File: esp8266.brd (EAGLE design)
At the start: 29.5 x 28.6 mm, 33 parts, among them IC1 74LVC1G08DBV, U1 FT232RL-BASICSSOP, U2 SPX3819M5-L33

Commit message: Change the second VIN to ground
It's more useful that way.
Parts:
- removed U$1: P-CHANNEL-MOSFET, GeekAmmo:SOT23-3
- added PFET1: P-CHANNEL-MOSFET, GeekAmmo:SOT23-3
- added PFET2: BSS84, transistor-small-signal:SOT23
- moved D2 3.35 mm to (23.0, 71.8), turned to 180 degrees
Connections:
- new net N$5: BAT.1, PFET2.3
- net GND: now also BAT.2, JP3.1, PFET2.1; no longer BAT.1
- net N$2: now also PFET1.1; no longer U$1.1
- net VBAT: now also PFET1.3, PFET2.2; no longer BAT.2, U$1.3
- net VIN: no longer JP3.1
- net VRIN: now also PFET1.2; no longer U$1.2
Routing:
- net GND: track 53.9 -> 18.4 mm, vias 17 -> 21
- net N$5: track 0.00 -> 10.3 mm
- net VRIN: track 33.3 -> 42.9 mm, vias 3 -> 4
- net RTS: track 42.0 -> 50.4 mm, vias 2 -> 4
- net N$2: track 75.5 -> 80.8 mm, vias 2 -> 7
- net VBAT: track 17.2 -> 21.7 mm, vias 0 -> 2
- net RX: track 39.4 -> 43.0 mm, vias 4 -> 2
- net VIN: track 72.8 -> 71.8 mm
- net 3V3: track 100.8 -> 101.4 mm
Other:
- board text added: "28.10.2015.HSF+LF"
- board text removed: "29.09.2015.HSF+LF"

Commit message: New routing
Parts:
- moved PFET2 1.42 mm to (20.3, 76.8)
- turned C1 to 0 degrees
- turned C4 to 90 degrees
- turned R13 to 90 degrees
- turned R3 to 180 degrees
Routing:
- net VRIN: track 42.9 -> 92.8 mm, vias 4 -> 6
- net VIN: track 71.8 -> 40.6 mm, vias 3 -> 2
- net RX: track 43.0 -> 19.2 mm, vias 2 -> 1
- net 3V3: track 101.4 -> 83.3 mm
- net CH_PD: track 15.1 -> 28.3 mm
- net GND: track 18.4 -> 5.17 mm, vias 21 -> 14
- net TX: track 38.4 -> 27.1 mm, vias 2 -> 1
- net RTS: track 50.4 -> 40.8 mm, vias 4 -> 1
- net RXLED: track 19.6 -> 11.0 mm
- net D-: track 10.7 -> 15.4 mm
- net VBAT: track 21.7 -> 26.5 mm
- net N$8: track 11.8 -> 7.37 mm
- net P14: track 12.7 -> 16.8 mm, vias 1 -> 0
- net N$4: track 11.8 -> 9.12 mm
- net ADC: track 17.1 -> 19.7 mm, vias 0 -> 2
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
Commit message: Finished routing
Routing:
- net RX: track 19.2 -> 20.7 mm
- net GND: track 5.17 -> 4.57 mm
- net P12: track 19.0 -> 18.5 mm, vias 1 -> 0
- net 3V3: track 83.3 -> 83.4 mm, vias 3 -> 5

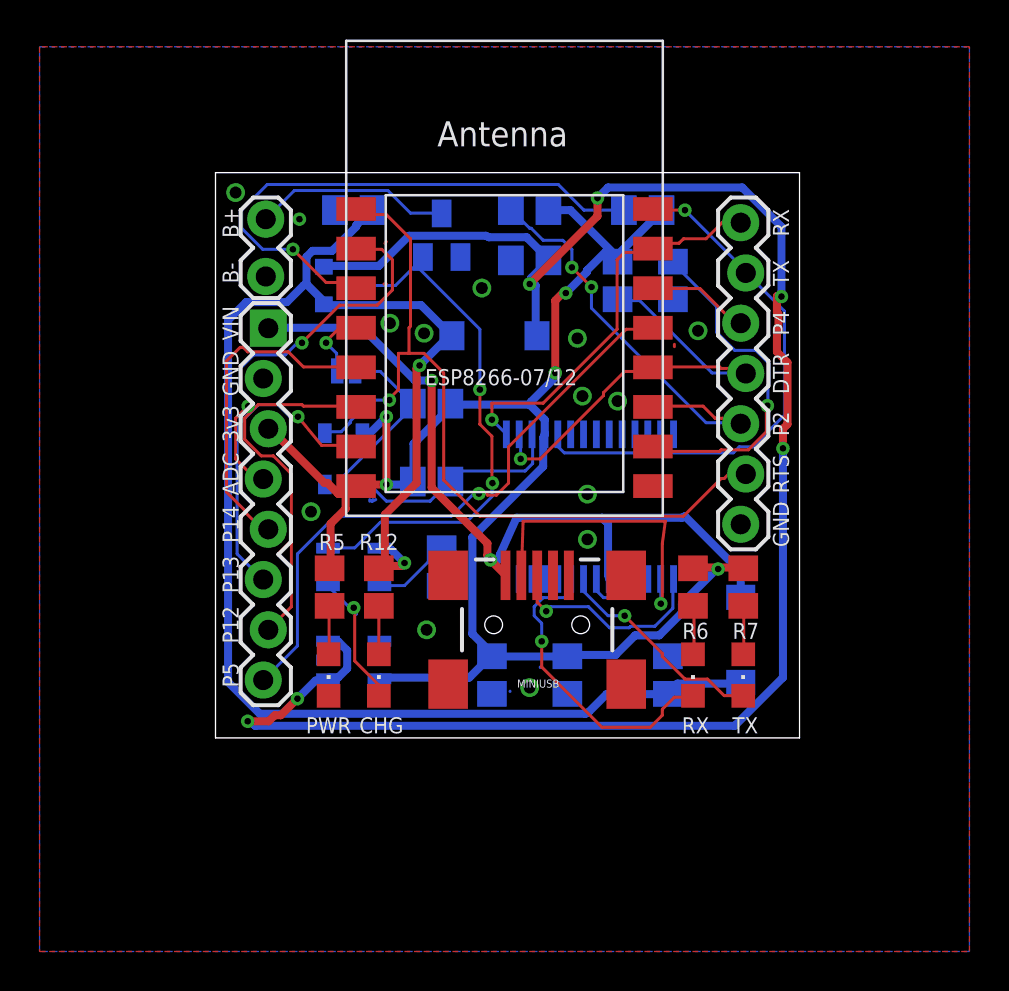
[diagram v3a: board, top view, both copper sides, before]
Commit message: Fix clearence issues
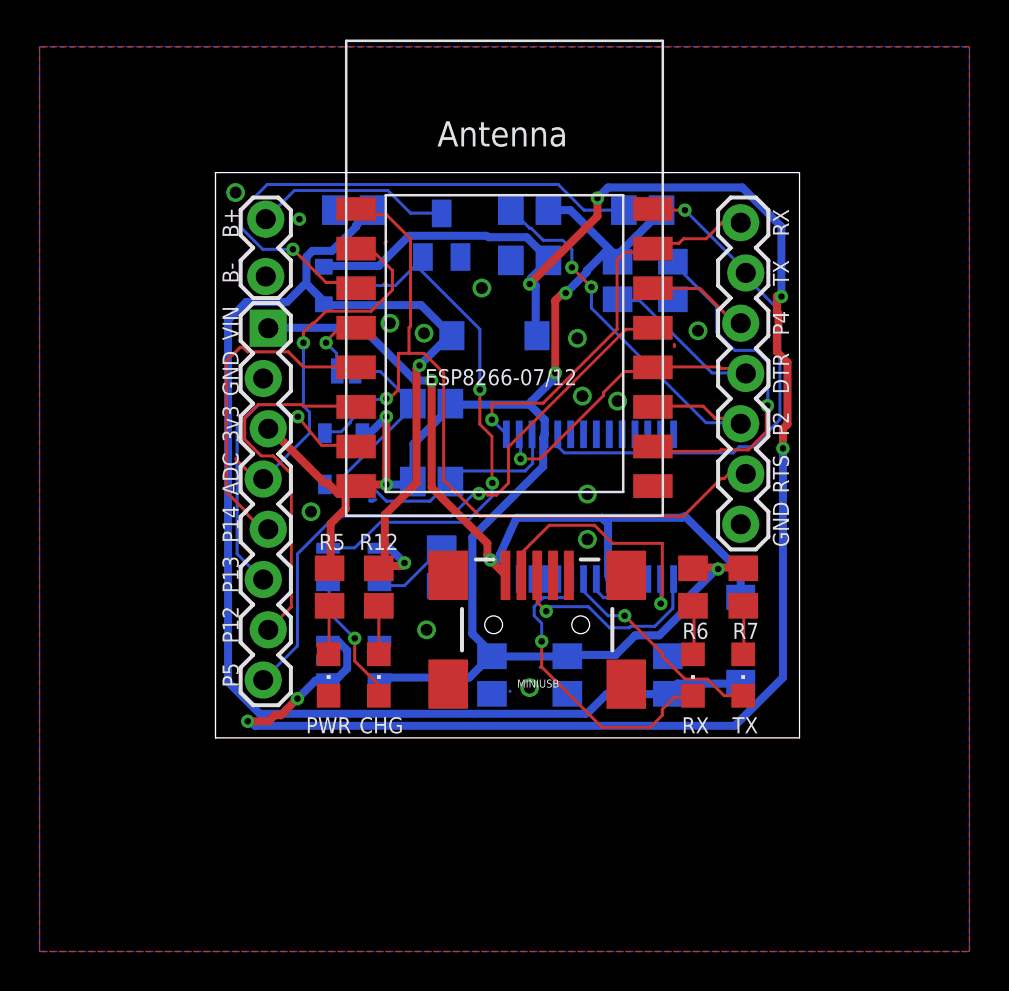
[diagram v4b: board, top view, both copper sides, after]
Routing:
- net ADC: track 19.8 -> 19.0 mm, vias 2 -> 1
- net D-: track 15.4 -> 14.7 mm
- net N$8: track 7.37 -> 6.70 mm
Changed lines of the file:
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@@
 <wire x1="35.3568" y1="66.1416" x2="35.052" y2="65.8368" width="0.1524" layer="16"/>
 <wire x1="36.0426" y1="66.1416" x2="35.3568" y2="66.1416" width="0.1524" layer="16"/>
-<wire x1="37.6428" y1="67.7418" x2="36.0426" y2="66.1416" width="0.1524" layer="16"/>
-<wire x1="37.6428" y1="72.9996" x2="37.6428" y2="67.7418" width="0.1524" layer="16"/>
-<wire x1="35.7378" y1="74.9046" x2="37.6428" y2="72.9996" width="0.1524" layer="16"/>
 <wire x1="26.2128" y1="66.7512" x2="26.188" y2="66.775" width="0.1524" layer="16"/>
 <wire x1="35.7378" y1="74.9046" x2="35.687" y2="74.93" width="0.1524" layer="16"/>
@@
 <wire x1="35.7378" y1="74.9808" x2="35.687" y2="74.93" width="0.1524" layer="16"/>
 <via x="32.6136" y="78.105" extent="1-16" drill="0.3302"/>
+<wire x1="37.4142" y1="67.5132" x2="36.0426" y2="66.1416" width="0.1524" layer="16"/>
+<wire x1="37.4142" y1="72.9996" x2="37.4142" y2="67.5132" width="0.1524" layer="16"/>
+<wire x1="35.7378" y1="74.676" x2="37.4142" y2="72.9996" width="0.1524" layer="16"/>
+<wire x1="35.7378" y1="74.8284" x2="35.7378" y2="74.676" width="0.1524" layer="16"/>
+<wire x1="35.7378" y1="74.8284" x2="35.687" y2="74.93" width="0.1524" layer="16"/>
 </signal>
 <signal name="P14">
@@
 <contactref element="ESP8266-07/12" pad="2"/>
 <contactref element="JP1" pad="4"/>
-<wire x1="17.2974" y1="76.1238" x2="16.002" y2="76.1238" width="0.1524" layer="1"/>
-<wire x1="17.8308" y1="75.5904" x2="17.2974" y2="76.1238" width="0.1524" layer="1"/>
-<wire x1="17.8308" y1="74.0664" x2="17.8308" y2="75.5904" width="0.1524" layer="1"/>
-<wire x1="17.0688" y1="73.3044" x2="17.8308" y2="74.0664" width="0.1524" layer="1"/>
-<wire x1="15.1638" y1="73.3044" x2="17.0688" y2="73.3044" width="0.1524" layer="1"/>
-<wire x1="13.2588" y1="71.3994" x2="15.1638" y2="73.3044" width="0.1524" layer="1"/>
-<wire x1="13.0302" y1="71.3994" x2="13.2588" y2="71.3994" width="0.1524" layer="16"/>
-<wire x1="12.4206" y1="70.7898" x2="13.0302" y2="71.3994" width="0.1524" layer="16"/>
-<wire x1="10.8204" y1="70.7898" x2="12.4206" y2="70.7898" width="0.1524" layer="16"/>
-<wire x1="10.1346" y1="70.104" x2="10.8204" y2="70.7898" width="0.1524" layer="16"/>
 <wire x1="10.8966" y1="64.5414" x2="9.906" y2="65.532" width="0.1524" layer="1"/>
 <wire x1="11.2776" y1="64.5414" x2="10.8966" y2="64.5414" width="0.1524" layer="1"/>
+<wire x1="11.2776" y1="64.5414" x2="11.303" y2="64.516" width="0.1524" layer="1"/>
+<wire x1="16.764" y1="76.1238" x2="16.002" y2="76.1238" width="0.1524" layer="1"/>
+<wire x1="17.8308" y1="75.057" x2="16.764" y2="76.1238" width="0.1524" layer="1"/>
+<wire x1="17.8308" y1="74.0664" x2="17.8308" y2="75.057" width="0.1524" layer="1"/>
+<wire x1="16.764" y1="72.9996" x2="17.8308" y2="74.0664" width="0.1524" layer="1"/>
+<wire x1="14.478" y1="72.9996" x2="16.764" y2="72.9996" width="0.1524" layer="1"/>
+<wire x1="13.8684" y1="72.39" x2="14.478" y2="72.9996" width="0.1524" layer="1"/>
+<wire x1="13.7922" y1="72.39" x2="13.8684" y2="72.39" width="0.1524" layer="1"/>
+<wire x1="13.335" y1="71.9328" x2="13.7922" y2="72.39" width="0.1524" layer="1"/>
+<wire x1="13.335" y1="71.3994" x2="13.335" y2="71.9328" width="0.1524" layer="1"/>
+<wire x1="13.335" y1="68.199" x2="13.335" y2="71.3994" width="0.1524" layer="16"/>
+<wire x1="13.6398" y1="67.8942" x2="13.335" y2="68.199" width="0.1524" layer="16"/>
+<wire x1="13.6398" y1="66.8274" x2="13.6398" y2="67.8942" width="0.1524" layer="16"/>
+<wire x1="11.3538" y1="64.5414" x2="13.6398" y2="66.8274" width="0.1524" layer="16"/>
 <wire x1="16.002" y1="76.1238" x2="15.995" y2="76.16" width="0.1524" layer="1"/>
-<wire x1="11.2776" y1="64.5414" x2="11.303" y2="64.516" width="0.1524" layer="1"/>
-<via x="13.2588" y="71.3994" extent="1-16" drill="0.3302"/>
-<via x="10.541" y="68.199" extent="1-16" drill="0.3302"/>
-<wire x1="9.906" y1="67.5894" x2="10.5156" y2="68.199" width="0.1524" layer="1"/>
-<wire x1="9.906" y1="65.532" x2="9.906" y2="67.5894" width="0.1524" layer="1"/>
-<wire x1="10.5156" y1="68.199" x2="10.541" y2="68.199" width="0.1524" layer="1"/>
-<wire x1="10.5156" y1="68.6562" x2="10.5156" y2="68.199" width="0.1524" layer="16"/>
-<wire x1="10.1346" y1="69.0372" x2="10.5156" y2="68.6562" width="0.1524" layer="16"/>
-<wire x1="10.1346" y1="70.104" x2="10.1346" y2="69.0372" width="0.1524" layer="16"/>
-<wire x1="10.5156" y1="68.199" x2="10.541" y2="68.199" width="0.1524" layer="16"/>
+<wire x1="11.3538" y1="64.5414" x2="11.303" y2="64.516" width="0.1524" layer="16"/>
+<via x="13.335" y="71.3994" extent="1-16" drill="0.3302"/>
 </signal>
 <signal name="WDOG">
@@
 <contactref element="CHG" pad="C"/>
 <contactref element="MCP73831" pad="1"/>
-<wire x1="16.002" y1="57.6834" x2="15.875" y2="58.0136" width="0.1524" layer="16"/>
-<wire x1="14.6304" y1="59.055" x2="16.002" y2="57.6834" width="0.1524" layer="16"/>
 <wire x1="14.6304" y1="59.055" x2="14.5749" y2="59.121" width="0.1524" layer="16"/>
-<via x="15.875" y="58.0136" extent="1-16" drill="0.3302"/>
 <wire x1="17.145" y1="54.102" x2="17.145" y2="53.56" width="0.1524" layer="1"/>
 <wire x1="15.9258" y1="55.3212" x2="17.145" y2="54.102" width="0.1524" layer="1"/>
-<wire x1="15.9258" y1="57.9882" x2="15.9258" y2="55.3212" width="0.1524" layer="1"/>
-<wire x1="15.9258" y1="57.9882" x2="15.875" y2="58.0136" width="0.1524" layer="1"/>
+<wire x1="14.6304" y1="57.7596" x2="14.6304" y2="58.9788" width="0.1524" layer="16"/>
+<wire x1="15.9258" y1="56.4642" x2="14.6304" y2="57.7596" width="0.1524" layer="16"/>
+<wire x1="15.9258" y1="55.3212" x2="15.9258" y2="56.4642" width="0.1524" layer="1"/>
+<wire x1="14.6304" y1="58.9788" x2="14.5749" y2="59.121" width="0.1524" layer="16"/>
+<via x="15.9258" y="56.4642" extent="1-16" drill="0.3302"/>
 </signal>
 <signal name="N$10">
@@
 <wire x1="15.6972" y1="67.437" x2="15.6972" y2="67.3608" width="0.1524" layer="16"/>
 <wire x1="16.764" y1="68.5038" x2="15.6972" y2="67.437" width="0.1524" layer="16"/>
-<wire x1="17.6784" y1="68.5038" x2="16.764" y2="68.5038" width="0.1524" layer="16"/>
-<wire x1="17.6784" y1="68.58" x2="17.6784" y2="68.5038" width="0.1524" layer="1"/>
+<wire x1="17.526" y1="68.58" x2="16.764" y2="68.5038" width="0.1524" layer="16"/>
+<wire x1="17.6784" y1="68.58" x2="17.526" y2="68.58" width="0.1524" layer="1"/>
 <wire x1="14.478" y1="66.9036" x2="14.417" y2="66.832" width="0.1524" layer="16"/>
-<via x="17.6784" y="68.5038" extent="1-16" drill="0.3302"/>
+<via x="17.526" y="68.58" extent="1-16" drill="0.3302"/>
 </signal>
 <signal name="VRIN" class="1">
@@
 <wire x1="31.4706" y1="58.293" x2="31.3944" y2="58.2168" width="0.1524" layer="1"/>
 <wire x1="31.4706" y1="61.2648" x2="31.4706" y2="58.293" width="0.1524" layer="1"/>
-<wire x1="31.623" y1="62.3824" x2="31.4706" y2="61.2648" width="0.1524" layer="1"/>
-<wire x1="24.4348" y1="62.3824" x2="31.623" y2="62.3824" width="0.1524" layer="1"/>
-<wire x1="24.384" y1="60.8076" x2="24.4348" y2="62.3824" width="0.1524" layer="1"/>
 <wire x1="24.384" y1="59.6646" x2="24.384" y2="60.8076" width="0.1524" layer="1"/>
 <wire x1="31.3944" y1="59.436" x2="31.388" y2="59.463" width="0.1524" layer="16"/>
 <wire x1="24.384" y1="59.6646" x2="24.346" y2="59.65" width="0.1524" layer="1"/>
 <via x="31.3944" y="58.2168" extent="1-16" drill="0.3302"/>
+<wire x1="28.956" y1="61.2648" x2="31.4706" y2="61.2648" width="0.1524" layer="1"/>
+<wire x1="28.0416" y1="62.1792" x2="28.956" y2="61.2648" width="0.1524" layer="1"/>
+<wire x1="25.7556" y1="62.1792" x2="28.0416" y2="62.1792" width="0.1524" layer="1"/>
+<wire x1="24.384" y1="60.8076" x2="25.7556" y2="62.1792" width="0.1524" layer="1"/>
+<wire x1="24.384" y1="60.8076" x2="24.346" y2="59.65" width="0.1524" layer="1"/>
 </signal>
 <signal name="D+">

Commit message: More clearance adjustments and labeling improvements
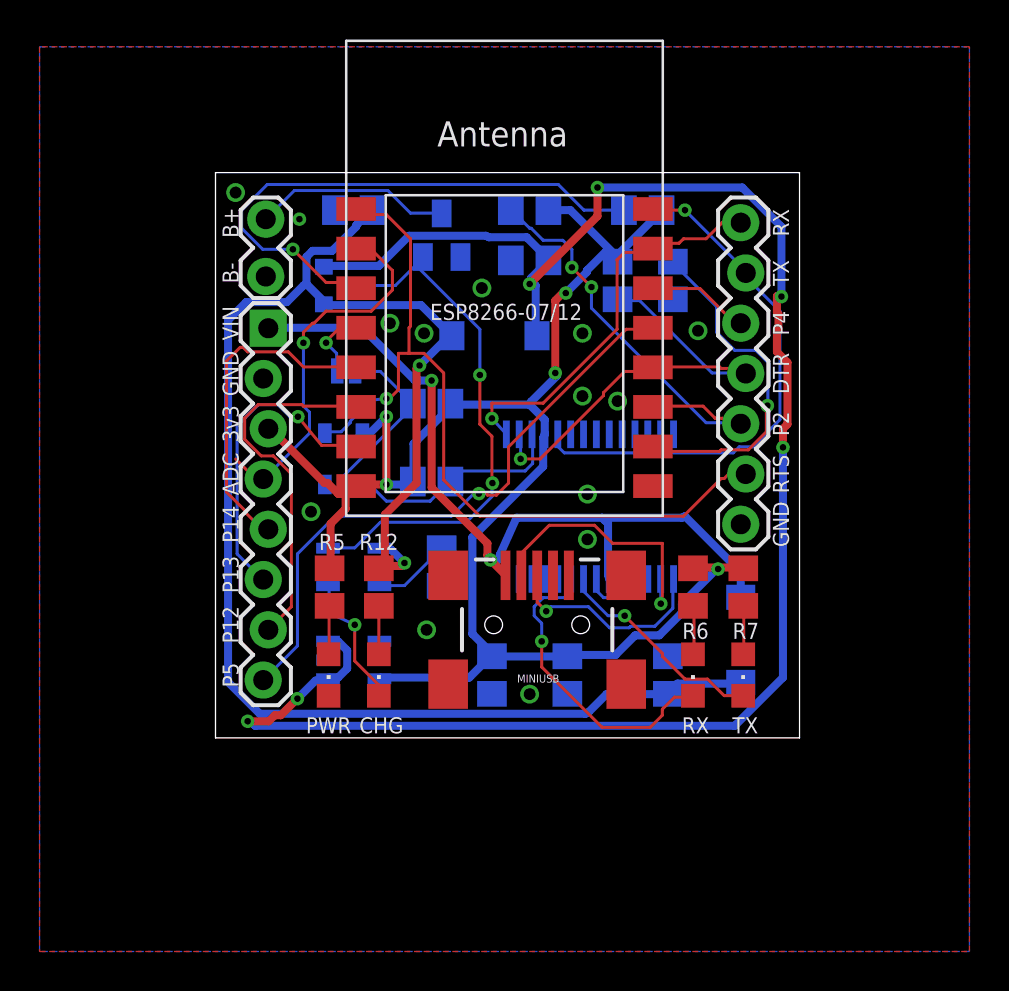
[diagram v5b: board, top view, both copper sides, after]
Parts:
- renumbered IC1 to AND, U2 to SPX
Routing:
- net GND: track 4.57 -> 3.80 mm
